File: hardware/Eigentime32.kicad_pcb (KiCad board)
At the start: 4 copper layers, 40 x 40 mm, 53 parts, among them J1 TC2030-NL, J2 AYF531035, Q1 DMG2305UX, SW2 BTN1, SW3 BTN2, U1 RV-3032-C7, U2 STM32L031G6U6, U3 TPS61099DRV, U5 TPS22916C, U6 SN74LV4T125, U7 SN74LV1T34, U8 ST25DV04KC-IE6C3, U9 CT8132SK-IS3

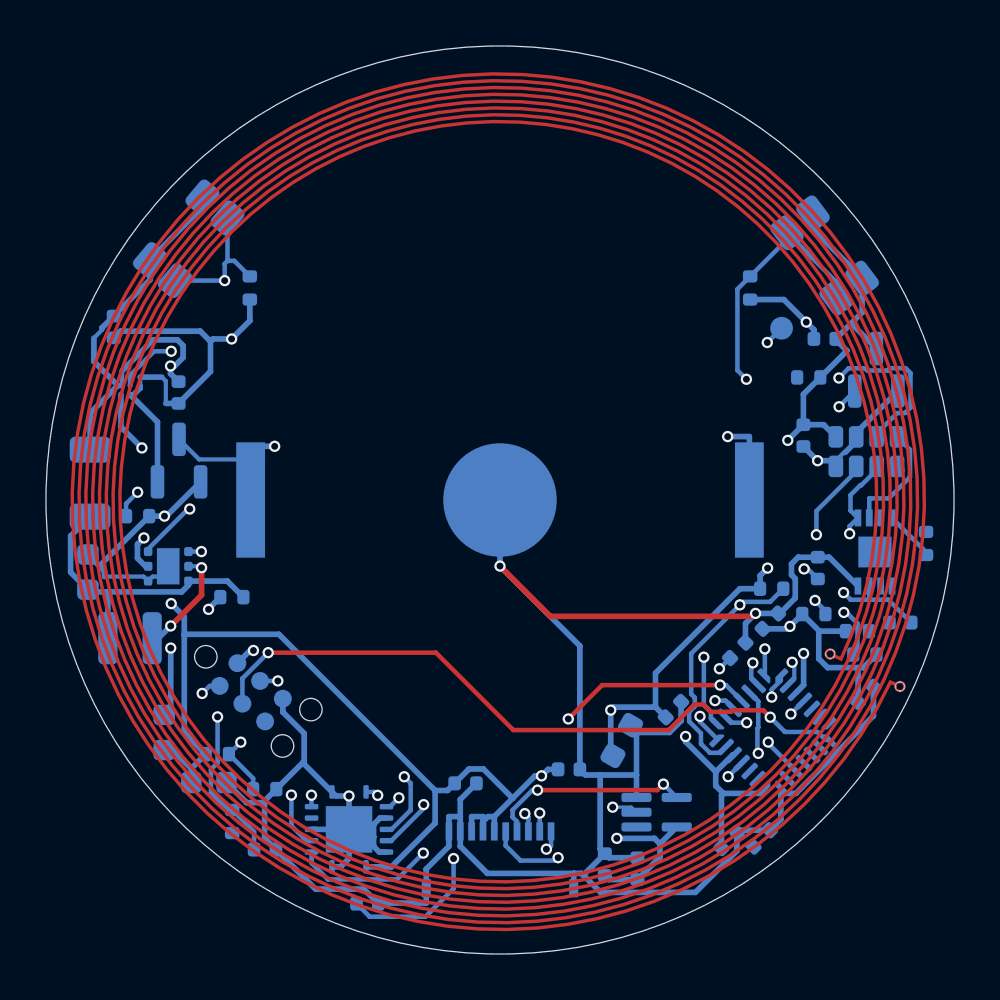
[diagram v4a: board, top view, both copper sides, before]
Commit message: Layout-4l: fully routed 4-layer board, LCD FPC folds under the glass
- JLC04081H-3313 stackup (0.8 mm, 4 layers), In1/In2 signal, no pours;
  coil-ring keep-out on F/In1/In2. 0.45/0.3 mm vias (JLC free tier).
- Routed: 0 unrouted, DRC clean (all severities), schematic parity clean.
  75 vias, ~930 mm of track; 0.2 mm signal / 0.25 mm power, 37 short
  necks at 0.15-0.19 mm between pads.
- LCD FPC folds 180 deg under the glass (Sharp LD-26X06A Fig. 8-2) into
  J2 on the front at 180 deg, pad row y=+7.55, Panasonic land pattern
  (pad 1 = SCLK at +X). Panel on a 1.2 mm frame. LCD buffers, pull-ups
  and NFC VCC decoupling moved to the front under the panel, over the
  cell area where vias are free.
- Boost cluster hand-placed and locked: single short SW track, output
  caps against VOUT with a direct GND return to U3 GND/EP.
- NFC corner: GND tucks under U8 to a via, AC0/AC1 run in parallel
  lanes to C22 and the coil terminals (no crossing inside the ring).
- I2C moved from PB6/PB7 to PA9/PA10 (both I2C1); schematic and pin
  table updated, ERC clean.
- Docs: stackup, price, J2/FPC geometry, assembly order, front-parts
  height zone. Renders updated.

Co-Authored-By: Claude Opus 5.5 (1M context) <noreply@anthropic.com>
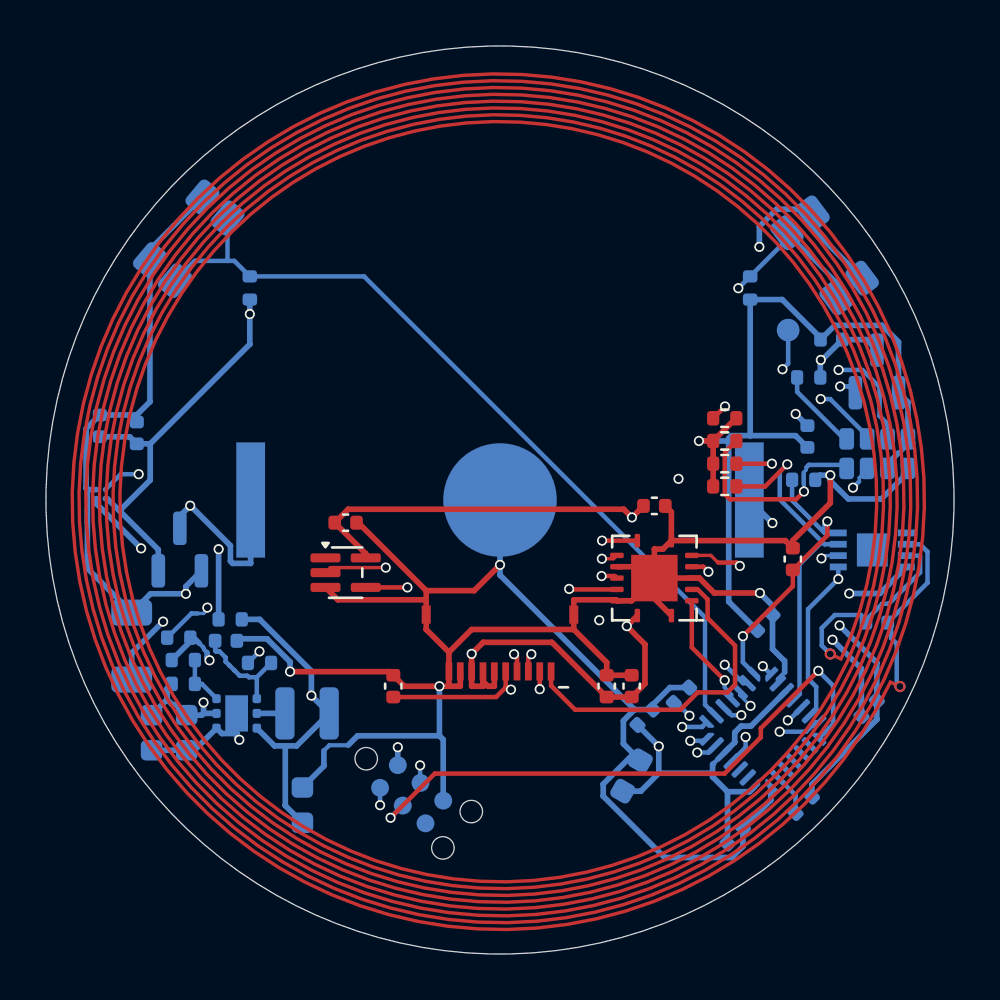
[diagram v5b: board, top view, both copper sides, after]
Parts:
- C16, C17, C18, C19, C20, C21, J2, R14, R6, R7, R8, U6, U7: moved to F.Cu
- moved U6 17.4 mm to (155.3, 108.4), turned to 180 degrees
- moved U7 17.3 mm to (141.7, 108.2)
- moved C16 14.8 mm to (155.3, 105.3)
- moved C17 14.7 mm to (141.7, 106.0)
- moved C4 13.9 mm to (139.8, 118.4)
- moved R6 12.1 mm to (158.4, 101.4)
- moved R7 10.2 mm to (158.4, 102.4)
- moved C20 9.64 mm to (143.8, 113.2), turned to 90 degrees
- moved C8 9.35 mm to (136.4, 111.2)
- moved L1 8.47 mm to (140.0, 114.4), turned to 180 degrees
- moved J1 8.37 mm to (144.6, 118.0)
- moved C19 8.04 mm to (154.3, 113.2)
- moved C18 7.86 mm to (153.2, 113.2)
- moved C2 7.41 mm to (132.3, 111.4)
- moved U3 7.14 mm to (136.9, 114.4)
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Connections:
- U2 pad 19: unconnected-(U2-PA9-Pad19) -> /SCL
- U2 pad 20: unconnected-(U2-PA10-Pad20) -> /SDA
- U2 pad 25: /SCL -> unconnected-(U2-PB6-Pad25)
- U2 pad 26: /SDA -> unconnected-(U2-PB7-Pad26)
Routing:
- net /MCU/SWDIO: track 0.91 -> 21.6 mm, vias 1 -> 2
- net /LCD_SCLK: track 25.3 -> 5.06 mm, vias 3 -> 1
- net /VBAT: track 116.7 -> 135.8 mm, vias 9 -> 5
- net /Power/FB: track 20.1 -> 2.27 mm, vias 2 -> 0
- net /SCL: track 5.05 -> 22.0 mm, vias 0 -> 3
- net /RTC_INT: track 19.3 -> 33.2 mm, vias 2 -> 3
- net /Power/VBST_IN: track 13.4 -> 25.0 mm, vias 0 -> 2
- net /MCU/BTN1_N: track 47.3 -> 36.6 mm, vias 2 -> 0
- net /Power/BST_EN: track 15.4 -> 4.70 mm, vias 2 -> 0
- net /MCU/NRST: track 30.1 -> 21.0 mm
- net /LCD/DISP: track 22.0 -> 13.5 mm, vias 3 -> 2
- net /NFC_GPO: track 7.06 -> 15.2 mm, vias 2 -> 1
- net /LCD_DISP: track 20.9 -> 13.5 mm
- net /NFC/AC0: track 0.00 -> 7.32 mm
- net /SDA: track 18.9 -> 26.2 mm
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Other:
- board text added: "FPC folds under the glass here, keep clear"
- board text added: "UNDER PANEL: 1.2 mm GAP, FRONT PARTS <= 1.0 mm HIGH"
